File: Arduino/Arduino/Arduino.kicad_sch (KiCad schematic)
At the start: 97 parts, among them J1 Conn_01x08_Socket, J2 Conn_01x08_Socket, J3 Conn_01x06_Socket, J4 Conn_01x10_Socket, J5 Conn_01x02_Socket, J6 Conn_02x03_Odd_Even, J7 Conn_02x03_Odd_Even, J8 Conn_01x02_Socket, J9 Conn_01x02_Socket, P1 USB_C_Plug_USB2.0, Q1 MMBT3904, Q2 MMBT3904, Q3 MMBT3904, Q4 MMBT3904, Q5 MMBT3904, Q6 MMBT3904, SW1 SW_Push, SW2 SW_Push, SW3 SW_Push, SW4 SW_Push, SW5 SW_Push, SW6 SW_Push, U1 LM1117DT-3.3, U2 TPS61087DSCR, U3 FT232RL, U4 ATxmega32A4U-A, U5 HC-05, U6 L293D

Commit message: Modificación de algunas huellas y arreglo de errores
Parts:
- removed P1: USB_C_Plug_USB2.0, symbol Connector:USB_C_Plug_USB2.0
- added J10: USB_B_Mini, Connector_USB:USB_Mini-B_Lumberg_2486_01_Horizontal, symbol Connector:USB_B_Mini
- C1, C3, C4, C5: footprint (none) -> Capacitor_SMD:CP_Elec_5x4.5
- C10, C11, C12, C14, C15, C16, C17, C18, C2, C6, C7, C8, C9: footprint (none) -> Capacitor_SMD:C_0805_2012Metric
- C13: value C -> 100nF; footprint (none) -> Capacitor_SMD:C_0805_2012Metric
- D1, D2: footprint (none) -> Diode_SMD:D_SMA
- D10, D11, D12, D3, D4, D6, D7, D8, D9: footprint (none) -> LED_SMD:LED_0805_2012Metric
- D13: footprint (none) -> LED_SMD:LED_RGB_5050-6
- J1, J2: footprint (none) -> Connector_PinSocket_2.54mm:PinSocket_1x08_P2.54mm_Vertical
- J3: footprint (none) -> Connector_PinSocket_2.54mm:PinSocket_1x06_P2.54mm_Vertical
- J4: footprint (none) -> Connector_PinSocket_2.54mm:PinSocket_1x10_P2.54mm_Vertical
- J5, J8, J9: footprint (none) -> Connector_PinSocket_2.54mm:PinSocket_1x02_P2.54mm_Vertical
- J6, J7: footprint (none) -> Connector_PinSocket_2.54mm:PinSocket_2x03_P2.54mm_Vertical
- L1: value L -> 5.6uH; footprint (none) -> Inductor_SMD:L_10.4x10.4_H4.8
- R1, R10, R11, R12, R13, R14, R15, R16, R17, R18, R19, R2, R20, R21, R22, R23, R24, R25, R26, R27, R28, R29, R3, R30, R31, R32, R33, R34, R35, R36, R4, R5, R6, R7, R8, R9: footprint (none) -> Resistor_SMD:R_0805_2012Metric
- RV1: footprint (none) -> Potentiometer_THT:Potentiometer_Runtron_RM-063_Horizontal
- SW1, SW2, SW3, SW4, SW5, SW6: footprint (none) -> Button_Switch_THT:SW_Tactile_Straight_KSA0Axx1LFTR
- U2: footprint TPS61087DSCR:IC_TPS61087DSCR -> TPS61087DRC:IC_TPS61087DSCR
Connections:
- net D+: now also J10.3 (D+)
- net D-: now also J10.2 (D-)
- net GND: now also J10.5 (GND), J10.SH (Shield)
- net VBUS: now also J10.1 (VBUS)
- no-connect marks 40 -> 39
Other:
- moved on the sheet: C1, C2, C3, C4, C5, C6, D1, D10, D11, D12, D13, D2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

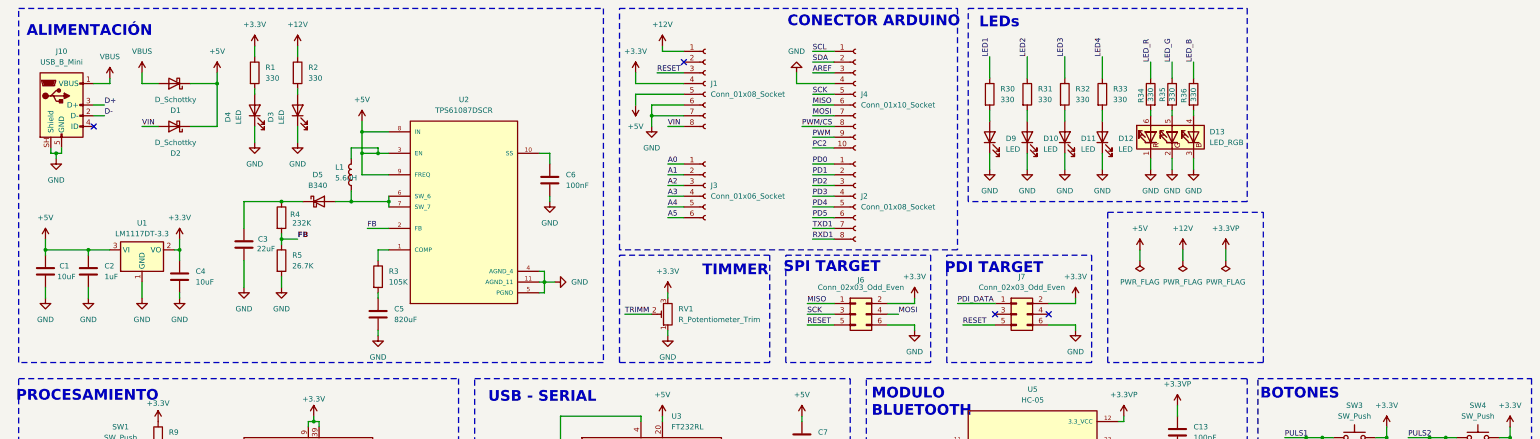
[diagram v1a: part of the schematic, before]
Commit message: Primera versión del Arduino sin completar el Ruteo
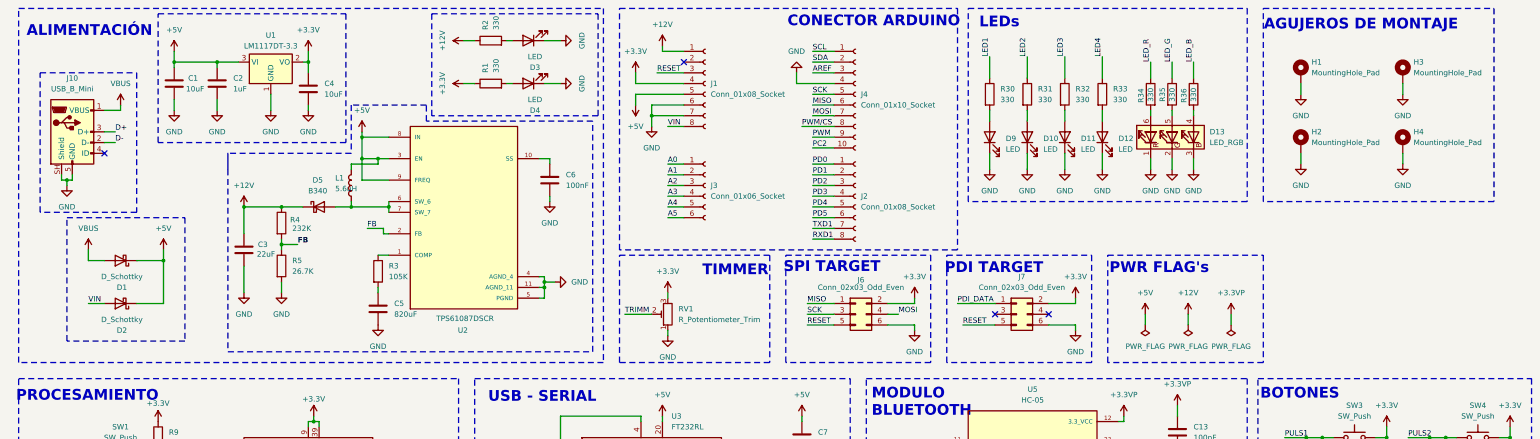
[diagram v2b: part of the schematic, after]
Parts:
- added H1, H2, H3, H4: MountingHole_Pad, MountingHole:MountingHole_3.2mm_M3_DIN965_Pad, symbol Mechanical:MountingHole_Pad
- D5: footprint Diode_SMD:D_SMC -> Diode_SMD:D_SMA
- SW1, SW2, SW3, SW4, SW5, SW6: footprint Button_Switch_THT:SW_Tactile_Straight_KSA0Axx1LFTR -> Button_Switch_SMD:SW_SPST_EVQP2_MiddlePushTravel_H2.5mm
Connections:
- net +12V: now also C3.1, D5.1 (K), R4.1
- net GND: now also H1.1, H2.1, H3.1, H4.1
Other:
- note added: "AGUJEROS DE MONTAJE"
- note added: "PWR FLAG's"
- moved on the sheet: C1, C2, C3, C4, C5, D1, D2, D3, D4, D5, J10, L1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

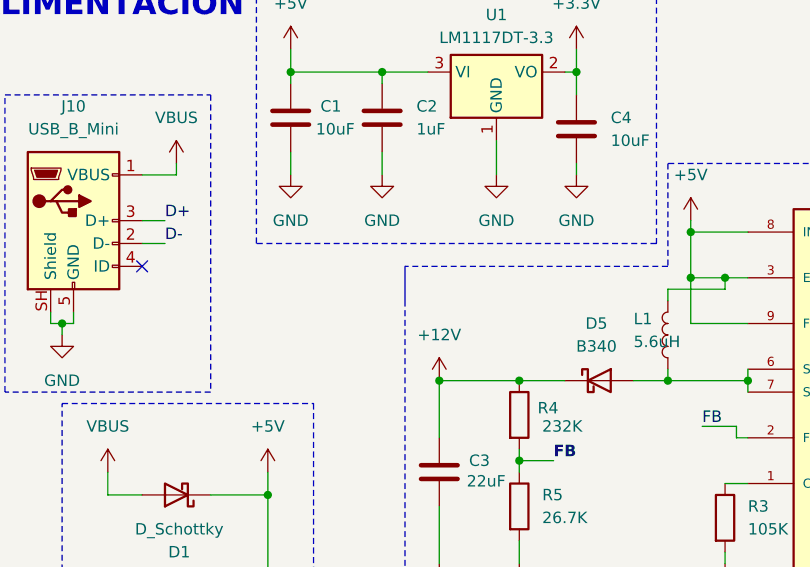
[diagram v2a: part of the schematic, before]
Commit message: Segunda Versión casi finalizada, falta enrutar detalles y gnd
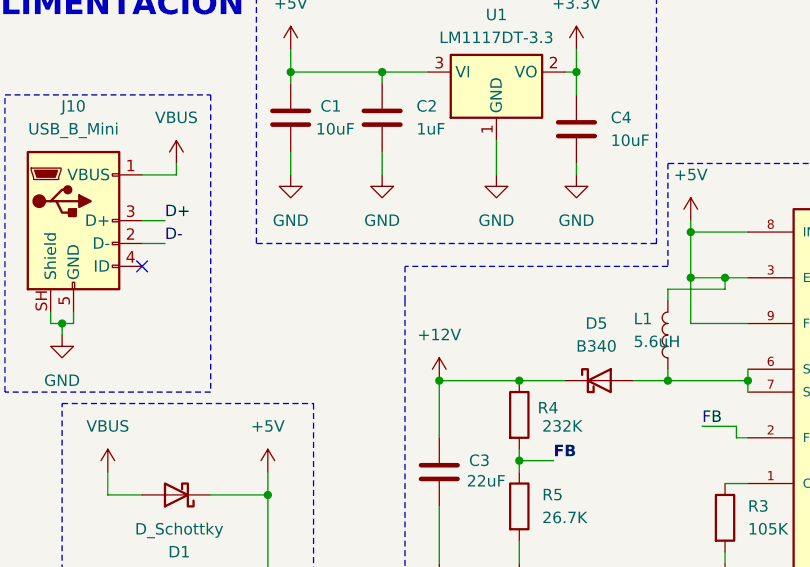
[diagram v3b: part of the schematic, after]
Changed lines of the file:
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@@
 		(stroke
 			(width 0)
-			(type default)
+			(type dash_dot)
+			(color 255 111 222 1)
 		)
 	)
